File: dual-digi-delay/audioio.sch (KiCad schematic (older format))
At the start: 10 parts, among them J27 AUDIO_IN, J28 MIX_OUT, J29 DELAY1_WET_OUT, J30 DELAY2_WET_OUT, SW2 Delay 2 Input

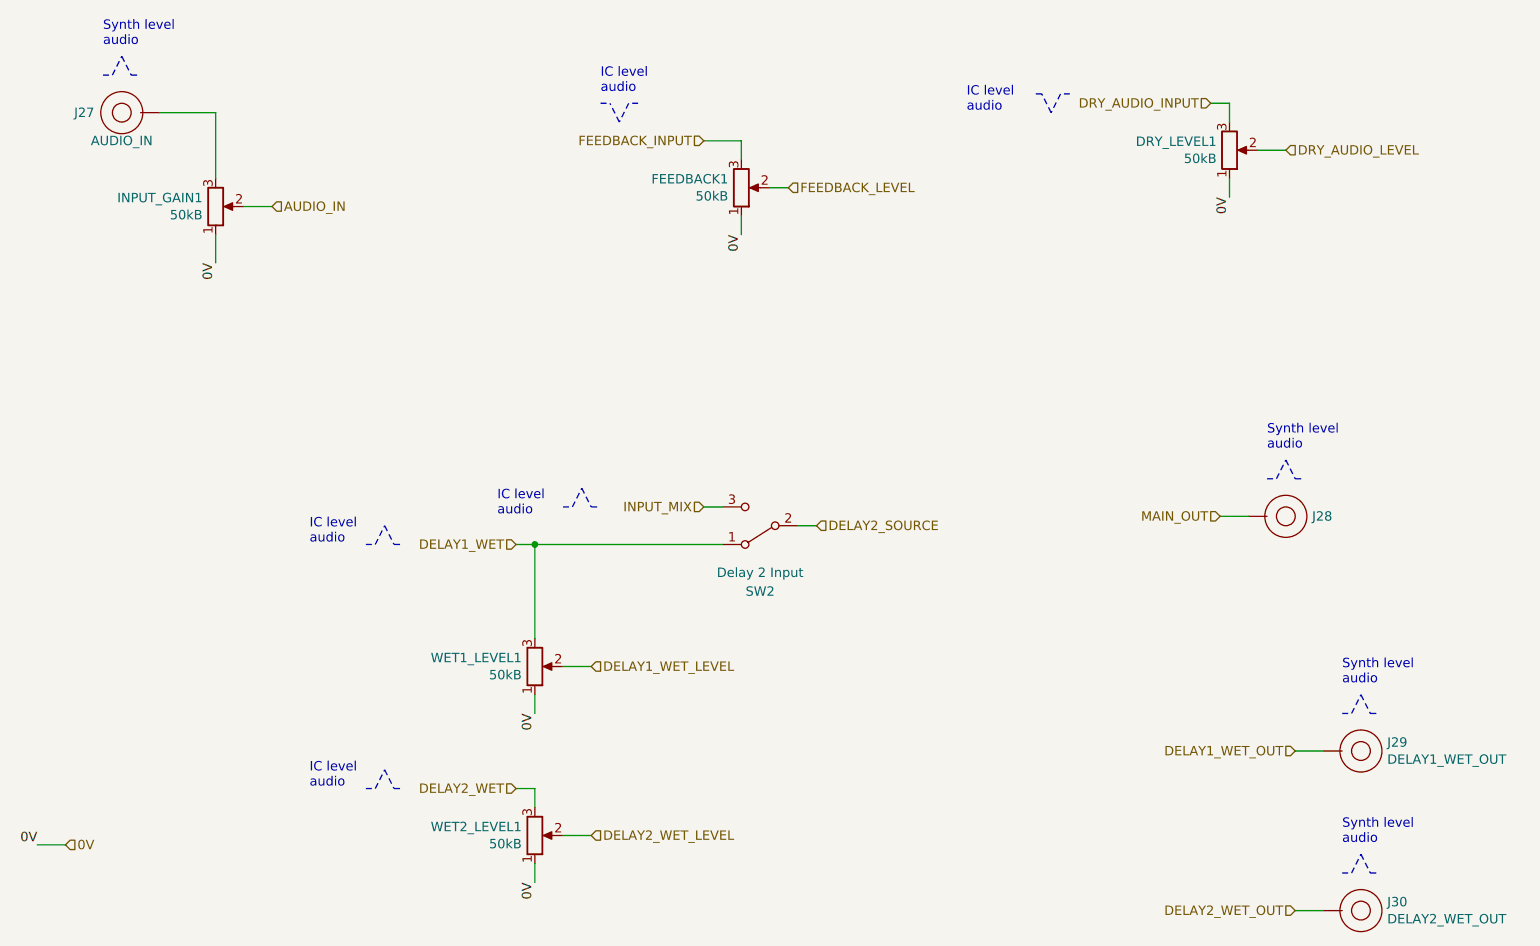
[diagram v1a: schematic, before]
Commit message: Updating digi delay to rev 2
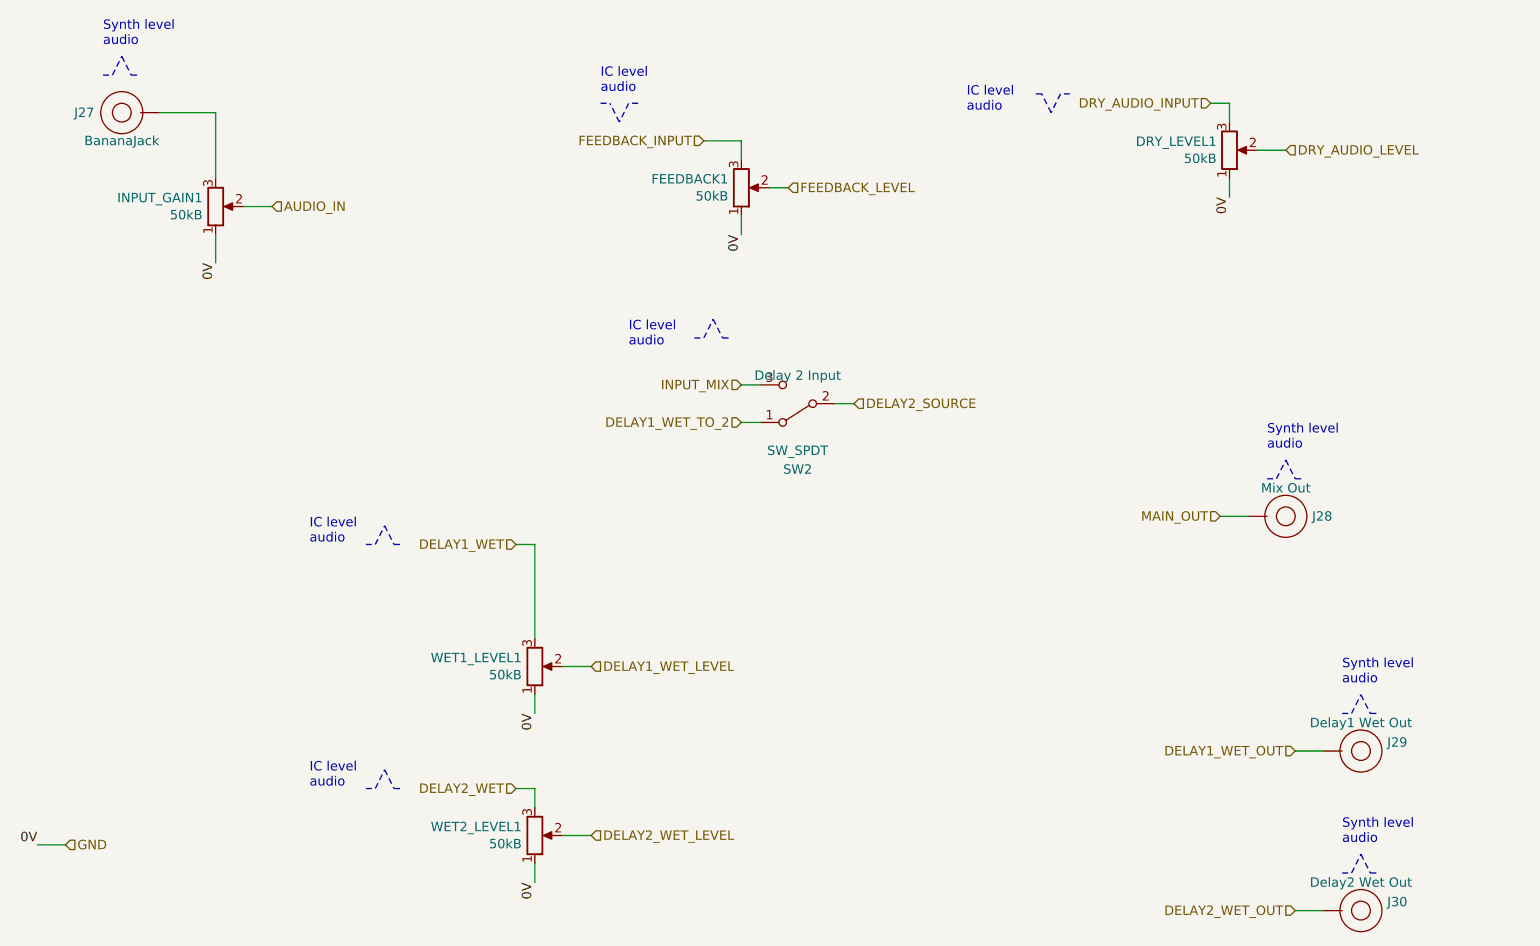
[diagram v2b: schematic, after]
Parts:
- DRY_LEVEL1, FEEDBACK1, INPUT_GAIN1, WET1_LEVEL1, WET2_LEVEL1: Vendor (none) -> Thonk
- J27: value AUDIO_IN -> BananaJack_PanelMount; Note (none) -> BananaJack; SKU (none) -> 108-0901-1; Vendor (none) -> Mouser
- J28: value MIX_OUT -> BananaJack_PanelMount; Note (none) -> Mix Out; SKU (none) -> 108-0901-1; Vendor (none) -> Mouser
- J29: value DELAY1_WET_OUT -> BananaJack_PanelMount; Note (none) -> Delay1 Wet Out; SKU (none) -> 108-0901-1; Vendor (none) -> Mouser
- J30: value DELAY2_WET_OUT -> BananaJack_PanelMount; Note (none) -> Delay2 Wet Out; SKU (none) -> 108-0901-1; Vendor (none) -> Mouser
- SW2: value Delay 2 Input -> SW_SPDT; Note (none) -> Delay 2 Input; SKU (none) -> 612-100SP1T1B3M2QEH; Vendor (none) -> Mouser
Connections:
- net DELAY1_WET: no longer SW2.1 (A)
- net 0V renamed GND
- new net DELAY1_WET_TO_2: SW2.1 (A)
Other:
- moved on the sheet: SW2
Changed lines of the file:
@@
 $Descr A4 11693 8268
 encoding utf-8
-Sheet 7 10
+Sheet 10 11
 Title "Dual PT2399 Digi Delay"
 Date ""
@@
 F 2 "rumblesan-footprints:Potentiometer_Alpha_RD901F-40-00D_Single_Vertical_CircularHoles" H 2350 2300 50  0001 C CNN
 F 3 "~" H 2350 2300 50  0001 C CNN
+F 4 "Thonk" H 2350 2300 50  0001 C CNN "Vendor"
 	1    2350 2300
 	1    0    0    1
@@
 P 1850 1800
 F 0 "J27" H 1650 1800 50  0000 C CNN
-F 1 "AUDIO_IN" H 1850 1650 50  0000 C CNN
+F 1 "BananaJack_PanelMount" H 1850 2025 50  0001 C CNN
 F 2 "rumblesan-footprints:BananaJack_THT_JohnsonCinch_108-09" H 1850 1500 50  0001 C CNN
 F 3 "" H 1850 1500 50  0001 C CNN
+F 4 "Mouser" H 1850 2175 50  0001 C CNN "Vendor"
+F 5 "108-0901-1" H 1850 2100 50  0001 C CNN "SKU"
+F 6 "BananaJack" H 1850 1650 50  0000 C CNN "Note"
 	1    1850 1800
 	1    0    0    -1
@@
 F 2 "rumblesan-footprints:Potentiometer_Alpha_RD901F-40-00D_Single_Vertical_CircularHoles" H 5150 2200 50  0001 C CNN
 F 3 "~" H 5150 2200 50  0001 C CNN
+F 4 "Thonk" H 5150 2200 50  0001 C CNN "Vendor"
 	1    5150 2200
 	1    0    0    1
@@
 F 2 "rumblesan-footprints:Potentiometer_Alpha_RD901F-40-00D_Single_Vertical_CircularHoles" H 4050 5650 50  0001 C CNN
 F 3 "~" H 4050 5650 50  0001 C CNN
+F 4 "Thonk" H 4050 5650 50  0001 C CNN "Vendor"
 	1    4050 5650
 	1    0    0    1
@@
 F 2 "rumblesan-footprints:Potentiometer_Alpha_RD901F-40-00D_Single_Vertical_CircularHoles" H 4050 4750 50  0001 C CNN
 F 3 "~" H 4050 4750 50  0001 C CNN
+F 4 "Thonk" H 4050 4750 50  0001 C CNN "Vendor"
 	1    4050 4750
 	1    0    0    1
@@
 F 2 "rumblesan-footprints:Potentiometer_Alpha_RD901F-40-00D_Single_Vertical_CircularHoles" H 7750 2000 50  0001 C CNN
 F 3 "~" H 7750 2000 50  0001 C CNN
+F 4 "Thonk" H 7750 2000 50  0001 C CNN "Vendor"
 	1    7750 2000
 	1    0    0    1
@@
 AR Path="/623586D0/623FAD28" Ref="J28"  Part="1"
 F 0 "J28" H 7910 3950 50  0000 R CNN
-F 1 "MIX_OUT" H 8050 3800 50  0001 C CNN
+F 1 "BananaJack_PanelMount" H 8050 3800 50  0001 C CNN
 F 2 "rumblesan-footprints:BananaJack_THT_JohnsonCinch_108-09" H 8050 3650 50  0001 C CNN
 F 3 "" H 8050 3650 50  0001 C CNN
+F 4 "Mouser" H 8050 4325 50  0001 C CNN "Vendor"
+F 5 "108-0901-1" H 8050 4250 50  0001 C CNN "SKU"
+F 6 "Mix Out" H 8050 3800 50  0000 C CNN "Note"
 	1    8050 3950
 	-1   0    0    1
@@
 L Switch:SW_SPDT SW?
 U 1 1 6240F9FA
-P 5250 4000
+P 5450 3350
 AR Path="/6240F9FA" Ref="SW?"  Part="1"
 AR Path="/623586D0/6240F9FA" Ref="SW2"  Part="1"
-F 0 "SW2" H 5250 4350 50  0000 C CNN
-F 1 "Delay 2 Input" H 5250 4250 50  0000 C CNN
-F 2 "rumblesan-footprints:Toggle_Switch_100SP1T1B3M2QE" H 5250 4000 50  0001 C CNN
-F 3 "~" H 5250 4000 50  0001 C CNN
-	1    5250 4000
+F 0 "SW2" H 5450 3700 50  0000 C CNN
+F 1 "SW_SPDT" H 5450 3600 50  0000 C CNN
+F 2 "rumblesan-footprints:Toggle_Switch_100SP1T1B3M2QE" H 5450 3350 50  0001 C CNN
+F 3 "~" H 5450 3350 50  0001 C CNN
+F 4 "Mouser" H 5450 3350 50  0001 C CNN "Vendor"
+F 5 "612-100SP1T1B3M2QEH" H 5450 3350 50  0001 C CNN "SKU"
+F 6 "Delay 2 Input" H 5450 3200 50  0000 C CNN "Note"
+	1    5450 3350
 	-1   0    0    1
 $EndComp
 Wire Wire Line
-	4950 3900 5050 3900
-Text Notes 3850 3950 0    50   ~ 0
-IC level\naudio
-Wire Notes Line
-	4350 3900 4400 3900
-Wire Notes Line
-	4300 3800 4350 3900
-Wire Notes Line
-	4250 3900 4300 3800
-Wire Notes Line
-	4200 3900 4250 3900
-Wire Wire Line
-	5450 4000 5550 4000
+	5150 3250 5250 3250
+Text Notes 4550 3050 0    50   ~ 0
+IC level\naudio
+Wire Notes Line
+	5050 3000 5100 3000
+Wire Notes Line
+	5000 2900 5050 3000
+Wire Notes Line
+	4950 3000 5000 2900
+Wire Notes Line
+	4900 3000 4950 3000
+Wire Wire Line
+	5650 3350 5750 3350
 $Comp
 L BananaJacks:BananaJack_PanelMount J?
@@
 AR Path="/623586D0/6241CACD" Ref="J30"  Part="1"
 F 0 "J30" H 8310 6004 50  0000 R CNN
-F 1 "DELAY2_WET_OUT" H 8310 6095 50  0000 R CNN
+F 1 "BananaJack_PanelMount" H 8450 6275 50  0001 R CNN
 F 2 "rumblesan-footprints:BananaJack_THT_JohnsonCinch_108-09" H 8450 5750 50  0001 C CNN
 F 3 "" H 8450 5750 50  0001 C CNN
+F 4 "108-0901-1" H 8450 6350 50  0001 C CNN "SKU"
+F 5 "Mouser" H 8450 6425 50  0001 C CNN "Vendor"
+F 6 "Delay2 Wet Out" H 8450 5900 50  0000 C CNN "Note"
 	1    8450 6050
 	-1   0    0    1
@@
 AR Path="/623586D0/6241CADF" Ref="J29"  Part="1"
 F 0 "J29" H 8310 5154 50  0000 R CNN
-F 1 "DELAY1_WET_OUT" H 8310 5245 50  0000 R CNN
+F 1 "BananaJack_PanelMount" H 8450 5425 50  0001 R CNN
 F 2 "rumblesan-footprints:BananaJack_THT_JohnsonCinch_108-09" H 8450 4900 50  0001 C CNN
 F 3 "" H 8450 4900 50  0001 C CNN
+F 4 "Mouser" H 8450 5575 50  0001 C CNN "Vendor"
+F 5 "108-0901-1" H 8450 5500 50  0001 C CNN "SKU"
+F 6 "Delay1 Wet Out" H 8450 5050 50  0000 C CNN "Note"
 	1    8450 5200
 	-1   0    0    1
@@
 	1550 5700 1400 5700
 Text HLabel 1550 5700 2    50   Input ~ 0
-0V
+GND
 Text Label 1400 5700 2    50   ~ 0
 0V
@@
 DELAY2_WET_OUT
 Wire Wire Line
-	4050 4100 5050 4100
-Connection ~ 4050 4100
-Wire Wire Line
 	4050 4100 4050 4600
-Text HLabel 4950 3900 0    50   Input ~ 0
+Text HLabel 5150 3250 0    50   Input ~ 0
 INPUT_MIX
-Text HLabel 5550 4000 2    50   Input ~ 0
+Text HLabel 5750 3350 2    50   Input ~ 0
 DELAY2_SOURCE
 Wire Wire Line
@@
 Wire Wire Line
 	8100 6050 8250 6050
+Text HLabel 5150 3450 0    50   Input ~ 0
+DELAY1_WET_TO_2
+Wire Wire Line
+	5250 3450 5150 3450
 $EndSCHEMATC
